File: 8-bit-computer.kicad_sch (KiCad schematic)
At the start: 1 part

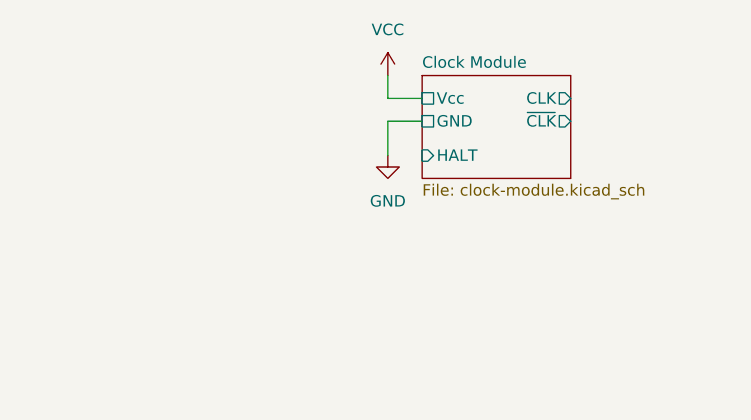
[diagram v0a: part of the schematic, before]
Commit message: Fix 74LS04N model and clock module simulation
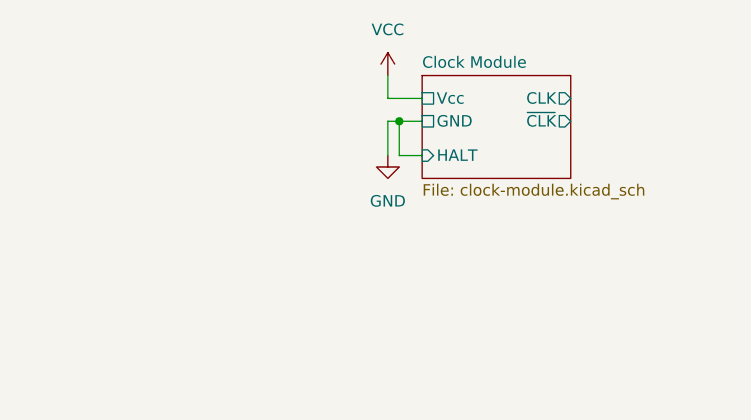
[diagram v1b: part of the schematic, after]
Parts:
- V1: now left out of the parts list
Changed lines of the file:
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@@
 		(comment 2 "https://eater.net/8bit")
 	)
+	(junction
+		(at 113.03 77.47)
+		(diameter 0)
+		(color 0 0 0 0)
+	)
 	(wire
 		(pts
@@
 	(wire
 		(pts
-			(xy 111.76 77.47) (xy 115.57 77.47)
+			(xy 111.76 77.47) (xy 113.03 77.47)
+		)
+		(stroke
+			(width 0)
+			(type default)
+		)
+	)
+	(wire
+		(pts
+			(xy 113.03 77.47) (xy 113.03 81.28)
 		)
 		(stroke
@@
 	(wire
 		(pts
+			(xy 115.57 81.28) (xy 113.03 81.28)
+		)
+		(stroke
+			(width 0)
+			(type default)
+		)
+	)
+	(wire
+		(pts
 			(xy 22.86 170.18) (xy 22.86 172.72)
+		)
+		(stroke
+			(width 0)
+			(type default)
+		)
+	)
+	(wire
+		(pts
+			(xy 113.03 77.47) (xy 115.57 77.47)
 		)
 		(stroke
@@
 		(unit 1)
 		(exclude_from_sim no)
-		(in_bom yes)
-		(on_board yes)
+		(in_bom no)
+		(on_board no)
 		(dnp no)
 		(fields_autoplaced yes)
@@
 		(unit 1)
 		(exclude_from_sim no)
-		(in_bom yes)
-		(on_board yes)
+		(in_bom no)
+		(on_board no)
 		(dnp no)
 		(fields_autoplaced yes)
@@
 		(unit 1)
 		(exclude_from_sim no)
-		(in_bom yes)
-		(on_board yes)
-		(dnp no)
-		(fields_autoplaced yes)
+		(in_bom no)
+		(on_board no)
+		(dnp no)
+		(fields_autoplaced yes)
